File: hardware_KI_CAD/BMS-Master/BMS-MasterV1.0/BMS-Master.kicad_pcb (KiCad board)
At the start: 4 copper layers, 202.7 x 136.3 mm, 330 parts, among them IC1 SN74LVC08AD, IC10 ACPL-217-56BE, IC11 ACPL-217-56BE, IC12 ACPL-217-56BE, IC13 ACPL-217-56BE, IC14 AQY-211EHA, IC15 M95M02-DRMN6TP, IC2 SN74LVC1G332DBVR, IC3 LS1205EF, IC4 SN74HC04DR, IC5 SN74LVC1G02DBVT, IC6 SN74LVC1G332DBVR, IC7 LS1205EF, IC8 ACPL-217-56BE, IC9 ACPL-217-56BE, J1 SMTU1632-LF.TR, J10 Conn_01x03_Pin, J11 436500327, J12 43045-0212, J13 43045-0212, J14 430450412, J15 43045-0212, J16 430450412, J17 430450412, J18 430450412, J19 430450412, J2 FTSH-110-01-L-DV-007, J20 DE9_Receptacle_MountingHoles, J21 DE9_Receptacle_MountingHoles, J22 43045-0212, J3 Conn_01x02_Pin, J4 FTSH-110-01-L-DV-007, J5 Conn_01x02_Pin, J6 430450412, J7 430450412, J8 Conn_01x03_Pin, J9 Conn_01x03_Pin, P1 USB_C_Plug_USB2.0, P2 USB_C_Plug_USB2.0, Q1 BSS84, Q2 BSS84, Q3 IRLML0100TRPBF, Q4 IRLML0100TRPBF, Q5 IRLML0100TRPBF, Q6 IRLML0100TRPBF, T1 HM2102NL, T2 HM2102NL, U1 STM32F429IIT6, U10 LTC6820HMS-PBF, U11 LTC6820HMS-PBF, U12 LTC6820HMS-PBF, U13 SN74LVC00AQPWRQ1, U14 SN74LVC00AQPWRQ1, U15 AD8628ARTZ-R2, U16 ADUM3300CRWZ, U17 TJA1052IT/5Y, U18 TJA1052IT/5Y, U19 IS42S16400J-7TLI, U2 ADR3425ARJZ-R2, U20 LM1085IS-3.3/NOPB, U21 TSR_2-2450, U3 ADUM3401CRWZ, U4 STM32F429VITx, U5 FT231XS-R, U6 FT231XS-R, U7 ADUM3401CRWZ, U8 ADUM3401CRWZ, U9 LTC6820HMS-PBF, Y1 ABS07-32.768KHZ-T, Y2 7B-8.000MAAJ-T, Y3 7B-8.000MAAJ-T

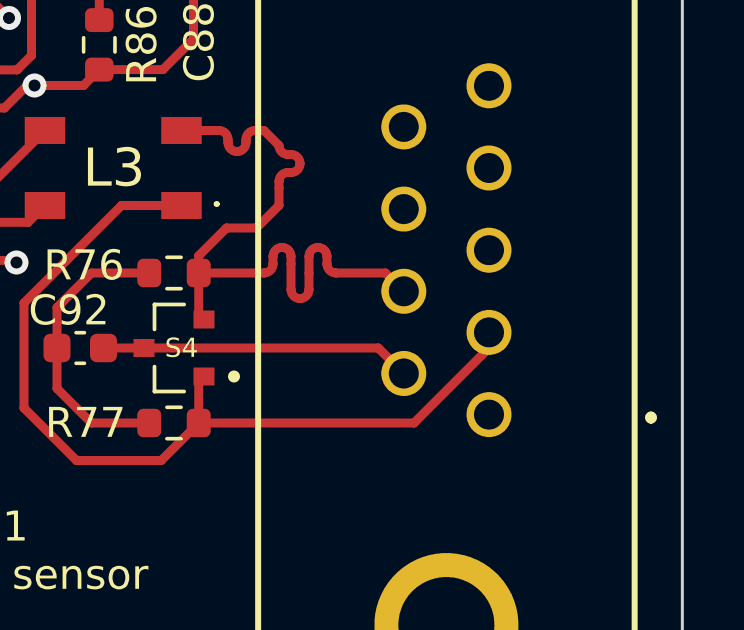
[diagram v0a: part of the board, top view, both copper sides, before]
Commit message: minor changes
changed some balancing values
changed so that default mode after bootup is standby instead of idle
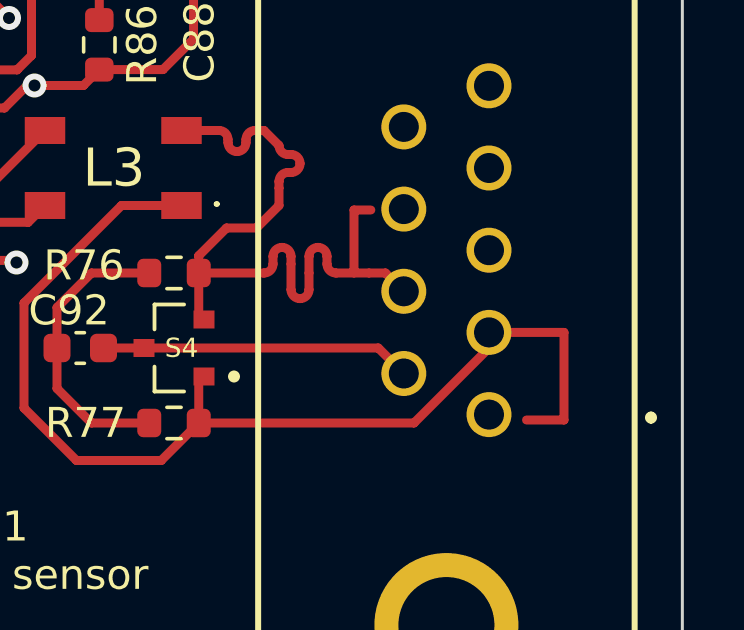
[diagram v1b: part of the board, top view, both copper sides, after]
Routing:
- net /CAN0_interface/CAN1_-: track 30.0 -> 36.7 mm
- net /CAN0_interface/CAN1_+: track 23.8 -> 26.4 mm
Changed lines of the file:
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@@
   (segment (start 269.598 201.652) (end 269.598 196.699) (width 0.381) (layer "B.Cu") (net 151))
   (segment (start 263.5 161.35) (end 266.325 161.35) (width 0.3) (layer "F.Cu") (net 154))
+  (segment (start 279.75 157.08) (end 279.75 160) (width 0.3) (layer "F.Cu") (net 154))
   (segment (start 274.75 160.1) (end 277.25 157.6) (width 0.3) (layer "F.Cu") (net 154))
   (segment (start 267.575 158.725) (end 267.75 158.55) (width 0.3) (layer "F.Cu") (net 154))
+  (segment (start 277.25 157.08) (end 279.75 157.08) (width 0.3) (layer "F.Cu") (net 154))
   (segment (start 266.325 161.35) (end 267.575 160.1) (width 0.3) (layer "F.Cu") (net 154))
   (segment (start 267.575 160.1) (end 267.575 158.725) (width 0.3) (layer "F.Cu") (net 154))
   (segment (start 261.75 156.1) (end 261.75 159.6) (width 0.3) (layer "F.Cu") (net 154))
+  (segment (start 279.75 160) (end 278.5 160) (width 0.3) (layer "F.Cu") (net 154))
   (segment (start 277.25 157.6) (end 277.25 157.08) (width 0.3) (layer "F.Cu") (net 154))
   (segment (start 265 152.85) (end 261.75 156.1) (width 0.3) (layer "F.Cu") (net 154))
@@
   (segment (start 271.85 154.547103) (end 271.85 154.8) (width 0.3) (layer "F.Cu") (net 156))
   (segment (start 267.575 156.475) (end 267.75 156.65) (width 0.3) (layer "F.Cu") (net 156))
+  (segment (start 272.75 155.1) (end 272.75 153) (width 0.3) (layer "F.Cu") (net 156))
+  (segment (start 272.15 155.1) (end 273.25 155.1) (width 0.3) (layer "F.Cu") (net 156))
   (segment (start 273.8 155.1) (end 274.41 155.71) (width 0.3) (layer "F.Cu") (net 156))
   (segment (start 270.65 154.547103) (end 270.65 154.8) (width 0.3) (layer "F.Cu") (net 156))
@@
   (segment (start 270.25 152.267833) (end 270.25 152.85) (width 0.3) (layer "F.Cu") (net 156))
   (segment (start 270.55 151.15) (end 270.651054 151.15) (width 0.3) (layer "F.Cu") (net 156))
-  (segment (start 272.15 155.1) (end 273.8 155.1) (width 0.3) (layer "F.Cu") (net 156))
+  (segment (start 273.25 155.1) (end 273.8 155.1) (width 0.3) (layer "F.Cu") (net 156))
   (segment (start 269.5 153.6) (end 268.5 153.6) (width 0.3) (layer "F.Cu") (net 156))
   (segment (start 270.05 154.8) (end 270.05 154.547103) (width 0.3) (layer "F.Cu") (net 156))
@@
   (segment (start 270.25 152.85) (end 269.5 153.6) (width 0.3) (layer "F.Cu") (net 156))
   (segment (start 269.45 150.35) (end 269.75 150.35) (width 0.3) (layer "F.Cu") (net 156))
+  (segment (start 272.75 153) (end 273.31 153) (width 0.3) (layer "F.Cu") (net 156))
   (arc (start 269.75 155.1) (mid 269.962132 155.012132) (end 270.05 154.8) (width 0.3) (layer "F.Cu") (net 156))
   (arc (start 268.85 151.051048) (mid 269.062132 150.96318) (end 269.15 150.751048) (width 0.3) (layer "F.Cu") (net 156))
